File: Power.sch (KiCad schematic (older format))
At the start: 26 parts

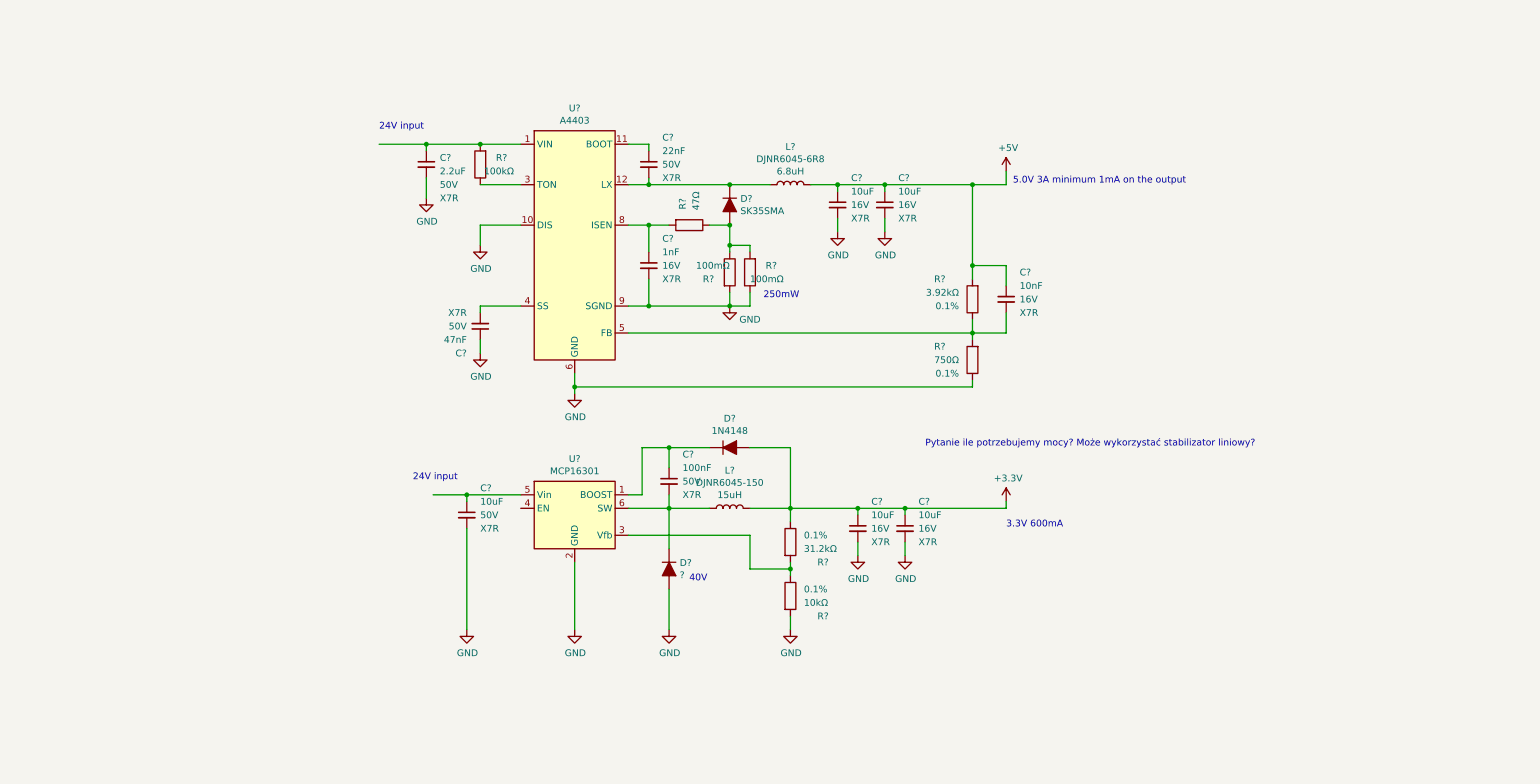
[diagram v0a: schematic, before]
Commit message: Finished Power Managment
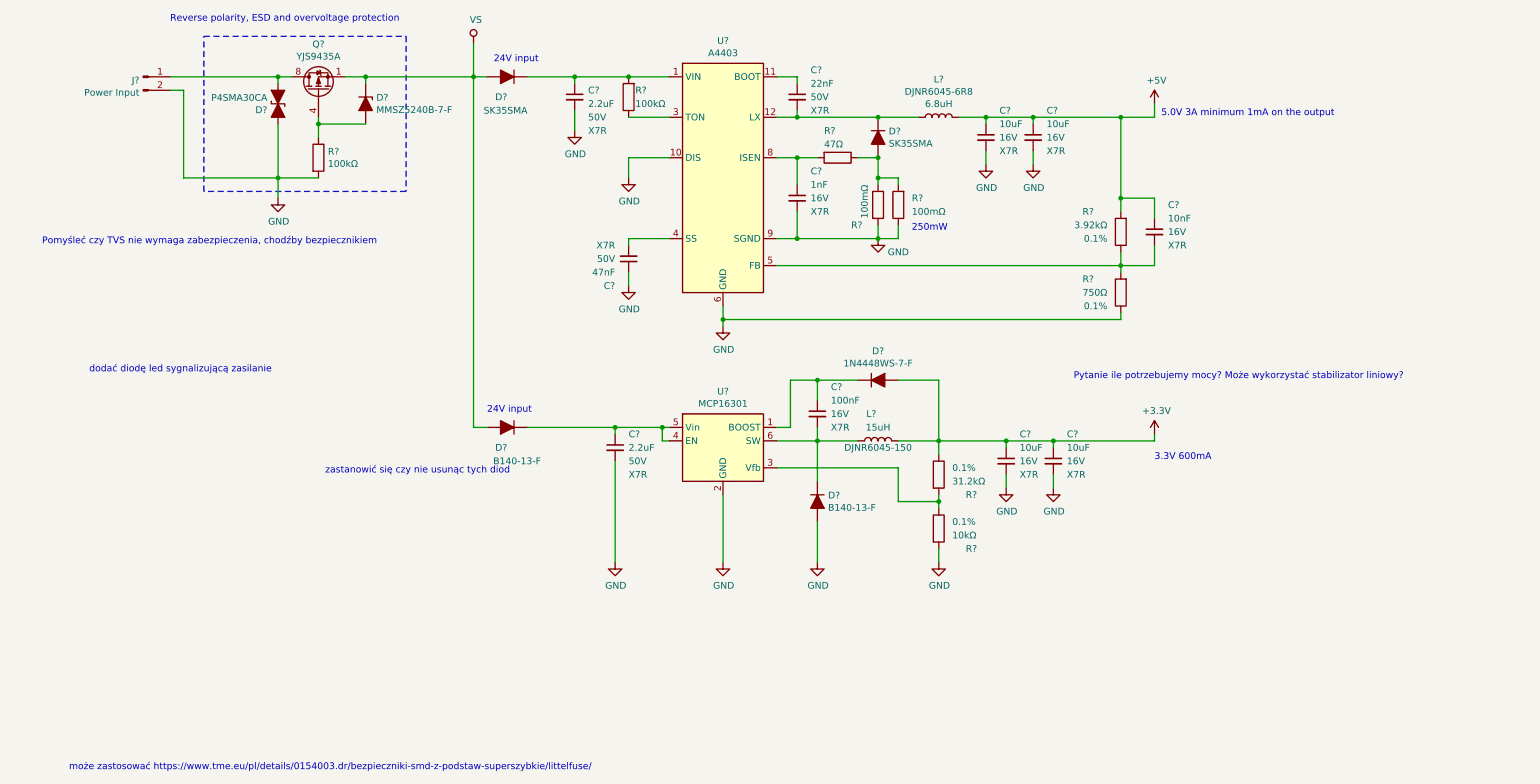
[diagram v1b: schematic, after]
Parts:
- added D?: SK35SMA, Diode_SMD:D_SMA, symbol Device:D_ALT
- added D?: B140-13-F, symbol Device:D_ALT
- added D?: MMSZ5240B-7-F, Diode_SMD:D_SOD-123, symbol Device:D_Zener_ALT
- added D?: P4SMA30CA, Diode_SMD:D_SMA, symbol Device:D_TVS_ALT
- added J?: Power Input, Connector_JST:JST_XH_B2B-XH-AM_1x02_P2.50mm_Vertical, symbol Connector:Conn_01x02_Male
- added Q?: YJS9435A, Package_SO:SOP-8_3.9x4.9mm_P1.27mm, symbol Library:YJS9435A
- added R?: 100kΩ, Resistor_SMD:R_0603_1608Metric, symbol Device:R
- C?: value 10uF -> 2.2uF
- C?: Napięcie 50V -> 16V
- D?: value ? -> B140-13-F
- D?: value 1N4148 -> 1N4448WS-7-F
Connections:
- net GND: now also D?.1 (A1), J?.2 (Pin_2), R?.2
- net at C?.1, R?.2, U?.1 (VIN): now also D?.1 (K)
- net at U?.4 (EN): now also C?.1, U?.5 (Vin), D?.1 (K)
- new net: D?.2 (A2), J?.1 (Pin_1), Q?.5 (D), Q?.6 (D), Q?.7 (D), Q?.8 (D)
- new net: D?.2 (A), Q?.4 (G), R?.1
- new net VS: D?.1 (K), D?.2 (A), D?.2 (A), Q?.1 (S), Q?.2 (S), Q?.3 (S)
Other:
- note added: "Pomyśleć czy TVS nie wymaga zabezpieczenia, chodźby bezpiecznikiem"
- note added: "Reverse polarity, ESD and overvoltage protection"
- note added: "dodać diodę led sygnalizującą zasilanie"
- note added: "może zastosować https://www.tme.eu/pl/details/0154003.dr/bezpieczniki-smd-z-podstaw-superszybkie/littelfuse/"
- note added: "zastanowić się czy nie usunąc tych diod"
- note removed: "40V"
- moved on the sheet: C?, D?, L?, R?, U?

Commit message: Finished Emergency Circuit
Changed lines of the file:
@@
 $Descr A4 11693 8268
 encoding utf-8
-Sheet 6 6
+Sheet 6 9
 Title ""
 Date ""
@@
 Text Notes 8900 4600 0    50   ~ 0
 3.3V 600mA
-Text Notes 8300 4000 0    50   ~ 0
+Text Notes 8000 4100 0    50   ~ 0
 Pytanie ile potrzebujemy mocy? Może wykorzystać stabilizator liniowy?
 $Comp
@@
 Wire Wire Line
 	5250 4350 4900 4350
-Text Notes 2750 4700 0    50   ~ 0
+Text Notes 2750 4750 0    50   ~ 0
 zastanowić się czy nie usunąc tych diod
-Text Notes 650  3000 0    50   ~ 0
+Text Notes 650  3200 0    50   ~ 0
 Pomyśleć czy TVS nie wymaga zabezpieczenia, chodźby bezpiecznikiem
 Text Notes 850  6900 0    50   ~ 0
 może zastosować https://www.tme.eu/pl/details/0154003.dr/bezpieczniki-smd-z-podstaw-superszybkie/littelfuse/
-Text Notes 1000 3950 0    50   ~ 0
+Text Notes 650  3350 0    50   ~ 0
 dodać diodę led sygnalizującą zasilanie
 $EndSCHEMATC

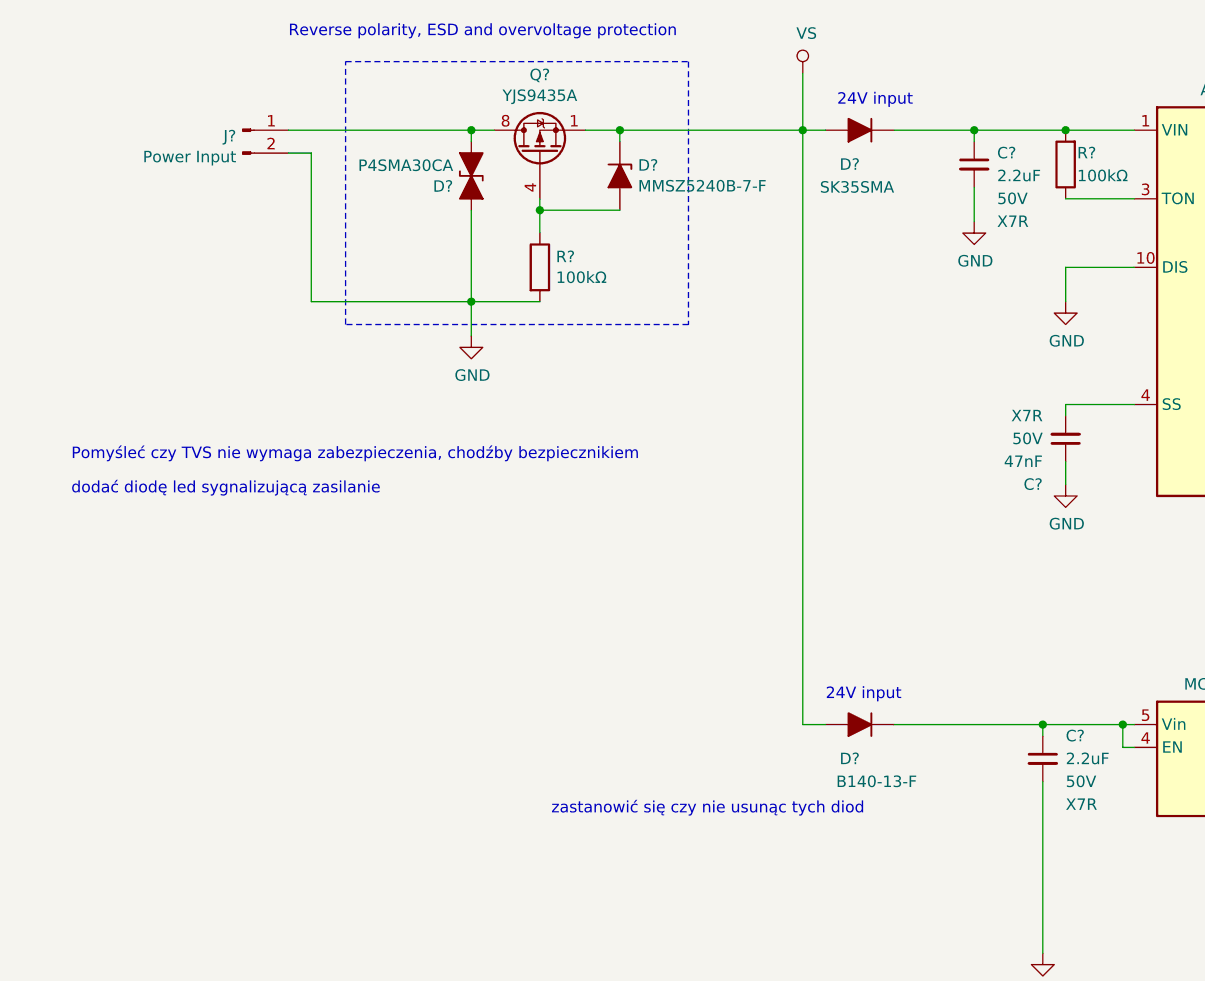
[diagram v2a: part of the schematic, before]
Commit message: Added Polyfuses and replace diodes
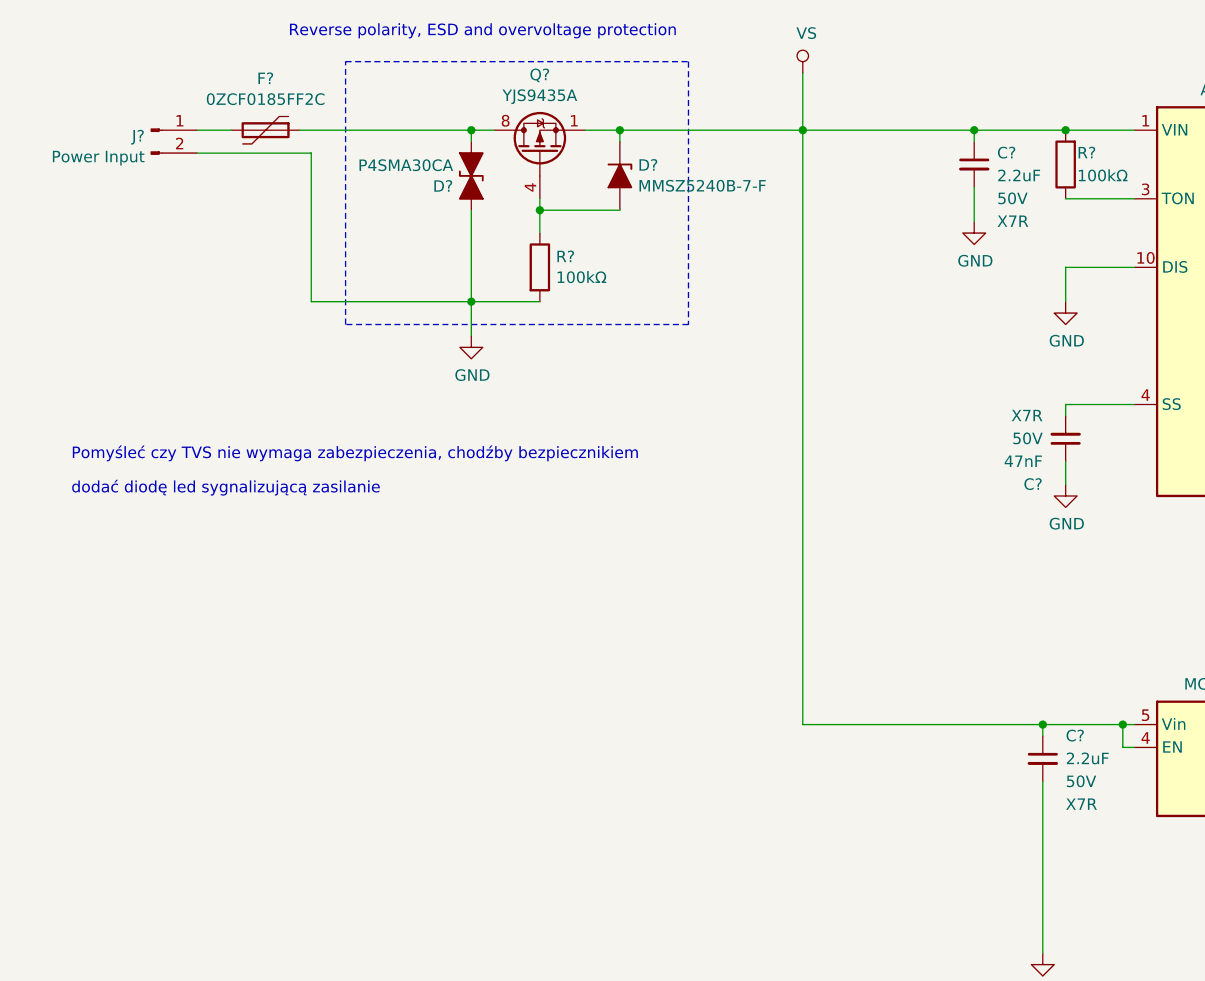
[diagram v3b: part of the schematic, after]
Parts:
- removed D?: SK35SMA, Diode_SMD:D_SMA, symbol Device:D_ALT
- removed D?: B140-13-F, symbol Device:D_ALT
- added F?: 0ZCF0185FF2C, Fuse:Fuse_2920_7451Metric, symbol Device:Polyfuse
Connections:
- net VS: now also C?.1, C?.1, R?.2, U?.1 (VIN), U?.4 (EN), U?.5 (Vin)
- net at D?.2 (A2), Q?.5 (D), Q?.6 (D)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: now also F?.1; no longer J?.1 (Pin_1)
- new net: F?.2, J?.1 (Pin_1)
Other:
- note removed: "24V input"
- note removed: "zastanowić się czy nie usunąc tych diod"
- moved on the sheet: J?
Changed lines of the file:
@@
 $Descr A4 11693 8268
 encoding utf-8
-Sheet 6 9
+Sheet 6 10
 Title ""
 Date ""
@@
 Wire Wire Line
 	4600 1800 4600 1750
-Wire Wire Line
-	4600 1750 4250 1750
 Connection ~ 4600 1750
-Text Notes 4000 1650 0    50   ~ 0
-24V input
 $Comp
 L power:GND #PWR?
@@
 Wire Wire Line
 	5700 4850 5700 5350
-Text Notes 3950 4250 0    50   ~ 0
-24V input
 $Comp
 L Device:L L?
@@
 	5300 4450 5250 4450
 $Comp
-L Device:D_ALT D?
-U 1 1 5E0EE1E1
-P 4100 1750
-F 0 "D?" H 4100 1900 50  0000 L CNN
-F 1 "SK35SMA" H 3950 2000 50  0000 L CNN
-F 2 "Diode_SMD:D_SMA" H 4100 1750 50  0001 C CNN
-F 3 "~" H 4100 1750 50  0001 C CNN
-	1    4100 1750
-	-1   0    0    1
-$EndComp
-$Comp
-L Device:D_ALT D?
-U 1 1 5E0EEA44
-P 4100 4350
-F 0 "D?" H 4100 4500 50  0000 L CNN
-F 1 "B140-13-F" H 3850 4600 50  0000 L CNN
-F 2 "" H 4100 4350 50  0001 C CNN
-F 3 "~" H 4100 4350 50  0001 C CNN
-	1    4100 4350
-	-1   0    0    1
-$EndComp
-Wire Wire Line
-	4250 4350 4900 4350
-Wire Wire Line
-	3950 4350 3850 4350
-$Comp
 L Connector:Conn_01x02_Male J?
 U 1 1 5E1237D9
-P 1400 1750
+P 1000 1750
 AR Path="/5E07245F/5E1237D9" Ref="J?"  Part="1"
 AR Path="/5DE588DC/5E1237D9" Ref="J?"  Part="1"
 AR Path="/5E1018C2/5E1237D9" Ref="J?"  Part="1"
-F 0 "J?" H 1372 1724 50  0000 R CNN
-F 1 "Power Input" H 1372 1633 50  0000 R CNN
-F 2 "Connector_JST:JST_XH_B2B-XH-AM_1x02_P2.50mm_Vertical" H 1400 1750 50  0001 C CNN
-F 3 "~" H 1400 1750 50  0001 C CNN
-	1    1400 1750
+F 0 "J?" H 972 1724 50  0000 R CNN
+F 1 "Power Input" H 972 1633 50  0000 R CNN
+F 2 "Connector_JST:JST_XH_B2B-XH-AM_1x02_P2.50mm_Vertical" H 1000 1750 50  0001 C CNN
+F 3 "~" H 1000 1750 50  0001 C CNN
+	1    1000 1750
 	1    0    0    -1
 $EndComp
@@
 	2400 1800 2400 1750
 Wire Wire Line
-	2400 1750 2500 1750
-Wire Wire Line
 	2400 2100 2400 2500
 Wire Wire Line
 	2400 2500 2700 2500
-Wire Wire Line
-	1600 1750 2400 1750
-Connection ~ 2400 1750
 $Comp
 L power:GND #PWR?
@@
 $EndComp
 Wire Wire Line
-	1600 1850 1700 1850
+	1200 1850 1700 1850
 Wire Wire Line
 	1700 1850 1700 2500
@@
 	3850 1750 3850 4350
 Connection ~ 3850 1750
-Wire Wire Line
-	3850 1750 3950 1750
 $Comp
 L power:VS #PWR?
@@
 Wire Wire Line
 	5250 4350 4900 4350
-Text Notes 2750 4750 0    50   ~ 0
-zastanowić się czy nie usunąc tych diod
 Text Notes 650  3200 0    50   ~ 0
 Pomyśleć czy TVS nie wymaga zabezpieczenia, chodźby bezpiecznikiem
@@
 Text Notes 650  3350 0    50   ~ 0
 dodać diodę led sygnalizującą zasilanie
+Wire Wire Line
+	3850 1750 4600 1750
+Wire Wire Line
+	3850 4350 4900 4350
+$Comp
+L Device:Polyfuse F?
+U 1 1 5E16A968
+P 1500 1750
+F 0 "F?" V 1275 1750 50  0000 C CNN
+F 1 " 0ZCF0185FF2C" V 1366 1750 50  0000 C CNN
+F 2 "Fuse:Fuse_2920_7451Metric" H 1550 1550 50  0001 L CNN
+F 3 "~" H 1500 1750 50  0001 C CNN
+	1    1500 1750
+	0    1    1    0
+$EndComp
+Wire Wire Line
+	1200 1750 1350 1750
+Wire Wire Line
+	1650 1750 2400 1750
+Connection ~ 2400 1750
+Wire Wire Line
+	2400 1750 2500 1750
 $EndSCHEMATC

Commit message: Improve schematics add new elements
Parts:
- added D? (x3): OF-SMD2012G-1, Diode_SMD:D_0805_2012Metric, symbol Device:LED_ALT
- added R?: 330Ω, symbol Device:R
- added R?: 1kΩ, symbol Device:R
- added R?: 10kΩ, Resistor_SMD:R_0805_2012Metric, symbol Device:R
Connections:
- net +3V3: now also R?.1
- net +5V: now also R?.1
- net GND: now also D?.1 (K), D?.1 (K), D?.1 (K)
- net VS: now also R?.1
- new net: D?.2 (A), R?.2 (x3)
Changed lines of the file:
@@
 Wire Wire Line
 	2400 1750 2500 1750
+$Comp
+L Device:R R?
+U 1 1 5E28FFAB
+P 2500 4850
+F 0 "R?" H 2570 4896 50  0000 L CNN
+F 1 "330Ω" H 2570 4805 50  0000 L CNN
+F 2 "" V 2430 4850 50  0001 C CNN
+F 3 "~" H 2500 4850 50  0001 C CNN
+	1    2500 4850
+	1    0    0    -1
+$EndComp
+Wire Wire Line
+	2500 5000 2500 5050
+$Comp
+L power:GND #PWR?
+U 1 1 5E299305
+P 2500 5450
+AR Path="/5DE588DC/5E299305" Ref="#PWR?"  Part="1"
+AR Path="/5DE587B9/5E299305" Ref="#PWR?"  Part="1"
+AR Path="/5E1018C2/5E299305" Ref="#PWR?"  Part="1"
+F 0 "#PWR?" H 2500 5200 50  0001 C CNN
+F 1 "GND" H 2505 5277 50  0000 C CNN
+F 2 "" H 2500 5450 50  0001 C CNN
+F 3 "" H 2500 5450 50  0001 C CNN
+	1    2500 5450
+	1    0    0    -1
+$EndComp
+Wire Wire Line
+	2500 5350 2500 5450
+Wire Wire Line
+	2500 4700 2500 4600
+$Comp
+L power:+3.3V #PWR?
+U 1 1 5E2A135E
+P 2500 4600
+F 0 "#PWR?" H 2500 4450 50  0001 C CNN
+F 1 "+3.3V" H 2515 4773 50  0000 C CNN
+F 2 "" H 2500 4600 50  0001 C CNN
+F 3 "" H 2500 4600 50  0001 C CNN
+	1    2500 4600
+	1    0    0    -1
+$EndComp
+$Comp
+L power:+5V #PWR?
+U 1 1 5E2A1F43
+P 2950 4600
+F 0 "#PWR?" H 2950 4450 50  0001 C CNN
+F 1 "+5V" H 2965 4773 50  0000 C CNN
+F 2 "" H 2950 4600 50  0001 C CNN
+F 3 "" H 2950 4600 50  0001 C CNN
+	1    2950 4600
+	1    0    0    -1
+$EndComp
+$Comp
+L Device:LED_ALT D?
+U 1 1 5E2A86AC
+P 2950 5200
+F 0 "D?" V 2989 5083 50  0000 R CNN
+F 1 "OF-SMD2012G-1" H 3300 5350 50  0000 R CNN
+F 2 "Diode_SMD:D_0805_2012Metric" H 2950 5200 50  0001 C CNN
+F 3 "~" H 2950 5200 50  0001 C CNN
+	1    2950 5200
+	0    -1   -1   0
+$EndComp
+$Comp
+L Device:R R?
+U 1 1 5E2A86B6
+P 2950 4850
+F 0 "R?" H 3020 4896 50  0000 L CNN
+F 1 "1kΩ" H 3020 4805 50  0000 L CNN
+F 2 "" V 2880 4850 50  0001 C CNN
+F 3 "~" H 2950 4850 50  0001 C CNN
+	1    2950 4850
+	1    0    0    -1
+$EndComp
+Wire Wire Line
+	2950 5000 2950 5050
+$Comp
+L power:GND #PWR?
+U 1 1 5E2A86C1
+P 2950 5450
+AR Path="/5DE588DC/5E2A86C1" Ref="#PWR?"  Part="1"
+AR Path="/5DE587B9/5E2A86C1" Ref="#PWR?"  Part="1"
+AR Path="/5E1018C2/5E2A86C1" Ref="#PWR?"  Part="1"
+F 0 "#PWR?" H 2950 5200 50  0001 C CNN
+F 1 "GND" H 2955 5277 50  0000 C CNN
+F 2 "" H 2950 5450 50  0001 C CNN
+F 3 "" H 2950 5450 50  0001 C CNN
+	1    2950 5450
+	1    0    0    -1
+$EndComp
+Wire Wire Line
+	2950 5350 2950 5450
+Wire Wire Line
+	2950 4700 2950 4600
+$Comp
+L Device:LED_ALT D?
+U 1 1 5E2B7376
+P 2050 5200
+F 0 "D?" V 2089 5083 50  0000 R CNN
+F 1 "OF-SMD2012G-1" H 2400 5350 50  0000 R CNN
+F 2 "Diode_SMD:D_0805_2012Metric" H 2050 5200 50  0001 C CNN
+F 3 "~" H 2050 5200 50  0001 C CNN
+	1    2050 5200
+	0    -1   -1   0
+$EndComp
+$Comp
+L Device:R R?
+U 1 1 5E2B7380
+P 2050 4850
+F 0 "R?" H 2120 4896 50  0000 L CNN
+F 1 "10kΩ" H 2120 4805 50  0000 L CNN
+F 2 "Resistor_SMD:R_0805_2012Metric" V 1980 4850 50  0001 C CNN
+F 3 "~" H 2050 4850 50  0001 C CNN
+	1    2050 4850
+	1    0    0    -1
+$EndComp
+Wire Wire Line
+	2050 5000 2050 5050
+$Comp
+L power:GND #PWR?
+U 1 1 5E2B738B
+P 2050 5450
+AR Path="/5DE588DC/5E2B738B" Ref="#PWR?"  Part="1"
+AR Path="/5DE587B9/5E2B738B" Ref="#PWR?"  Part="1"
+AR Path="/5E1018C2/5E2B738B" Ref="#PWR?"  Part="1"
+F 0 "#PWR?" H 2050 5200 50  0001 C CNN
+F 1 "GND" H 2055 5277 50  0000 C CNN
+F 2 "" H 2050 5450 50  0001 C CNN
+F 3 "" H 2050 5450 50  0001 C CNN
+	1    2050 5450
+	1    0    0    -1
+$EndComp
+Wire Wire Line
+	2050 5350 2050 5450
+Wire Wire Line
+	2050 4700 2050 4600
+$Comp
+L Device:LED_ALT D?
+U 1 1 5E28FB45
+P 2500 5200
+F 0 "D?" V 2539 5082 50  0000 R CNN
+F 1 "OF-SMD2012G-1" H 2850 5350 50  0000 R CNN
+F 2 "Diode_SMD:D_0805_2012Metric" H 2500 5200 50  0001 C CNN
+F 3 "~" H 2500 5200 50  0001 C CNN
+	1    2500 5200
+	0    -1   -1   0
+$EndComp
+$Comp
+L power:VS #PWR?
+U 1 1 5E2C2464
+P 2050 4600
+F 0 "#PWR?" H 1850 4450 50  0001 C CNN
+F 1 "VS" H 2067 4773 50  0000 C CNN
+F 2 "" H 2050 4600 50  0001 C CNN
+F 3 "" H 2050 4600 50  0001 C CNN
+	1    2050 4600
+	1    0    0    -1
+$EndComp
 $EndSCHEMATC
